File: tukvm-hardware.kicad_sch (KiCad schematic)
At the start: 19 parts, among them J1 PCIexpress_x1, J2 PCIexpress_bracket, J4 USB_C_Receptacle_USB2.0, U11 CH340N, U3 MCORE-H616

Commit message: Update pcb & sch for T113 SOM
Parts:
- removed R22: 33Ω, Resistor_SMD:R_0402_1005Metric, symbol Device:R_Small
- removed U3: MCORE-H616, tukvm:MCORE-H616, symbol tukvm:MCORE-H616
- added C23: 100uF 6.3V, Capacitor_SMD:C_1206_3216Metric, symbol Device:C_Small
- added C43: 10uF, Capacitor_SMD:C_0603_1608Metric, symbol Device:C_Small
- added SW1: SKRK, Button_Switch_SMD:SW_Push_SPST_NO_Alps_SKRK, symbol Switch:SW_Push
- added U3: TLT113-SOM, tukvm:SMD_140P_35X45_SOM_TLT113_PackageLength, symbol tukvm:TLT113-SOM
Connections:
- net +3.3V: now also C43.2, U3.135 (VDD_3V3_SOM)
- net +5V: now also C23.1, U3.139 (VDD_5V_SOM), U3.140 (VDD_5V_SOM)
- net ATX_PWR: now also U3.58 (PB2/LCD0_D0/I2S2_DOUT2/TWI0_SDA/I2S2_DIN2/LCD0_D18/UART4_TX/CAN0_TX0/PB_EINT2)
- net ATX_RST: now also U3.57 (PB12/DMIC_CLK/PWM0/SPDIF_IN/SPI1_CS/DBI_CSX/CLK_FANOUT2/IR_RX/PB_EINT12)
- net Earth: now also C23.2, C43.1, SW1.2, U3.106 (AGND_AUDIO), U3.116 (GND), U3.120 (GND), U3.128 (GND), U3.131 (GND), U3.134 (GND), U3.137 (GND), U3.138 (GND), U3.25 (GND), U3.33 (GND), U3.5 (GND), U3.52 (GND), U3.66 (GND), U3.71 (GND), U3.78 (GND), U3.85 (GND), U3.92 (GND), U3.97 (AGND_AUDIO)
- net HDD_LED: now also U3.46 (PE16/TWI3_SCK/D_JTAG_DO/PWM7/I2S0_BCLK/DMIC_DATA0/PE_EINT16)
- net HEART_BEAT_LED: now also U3.10 (PG8/UART1_RTS/TWI1_SCK/RGMII_RXD2/UART3_TX/PG_EINT8)
- net MS_STATUS: now also U3.91 (PD20/LCD0_HSYNC/TWI2_SCK/DMIC_CLK/PWM4/PD_EINT20)
- net MS_USBD+: now also U3.129 (USB1_DP)
- net MS_USBD-: now also U3.130 (USB1_DM)
- net OLED_SCL: now also U3.44 (PE14/TWI1_SCK/D_JTAG_MS/I2S0_DOUT1/I2S0_DIN0/DMIC_DATA2/RGMII_RXD3/PE_EINT14)
- net OLED_SDA: now also U3.45 (PE15/TWI1_SDA/D_JTAG_DI/PWM6/I2S0_LRCK/DMIC_DATA1/RGMII_RXCK/PE_EINT15)
- net OTG_D+: now also U3.132 (USB0_DP)
- net OTG_D-: now also U3.133 (USB0_DM)
- net PWR_LED: now also U3.47 (PE17/TWI3_SDA/D_JTAG_CK/IR_TX/I2S0_MCLK/DMIC_CLK/PE_EINT17)
- net SMCLK: now also U3.17 (PG6/UART1_TX/TWI2_SCK/RGMII_TXD2/PWM1/PG_EINT6)
- net SMDAT: now also U3.16 (PG7/UART1_RX/TWI2_SDA/RGMII_TXD3/SPDIF_IN/PG_EINT7)
- net TF_CLK: now also U3.29 (PF2/SDC0_CLK/UART0_TX/TWI0_SCK/LEDC_DO/SPDIF_IN/PF_EINT2)
- net TF_CMD: now also U3.31 (PF3/SDC0_CMD/JTAG_DO/R_JTAG_DO/I2S2_BCLK/PF_EINT3)
- net TF_D0: now also U3.28 (PF1/SDC0_D0/JTAG_DI/R_JTAG_DI/I2S2_DOUT0/I2S2_DIN1/PF_EINT1)
- net TF_D1: now also U3.27 (PF0/SDC0_D1/JTAG_MS/R_JTAG_MS/I2S2_DOUT1/I2S2_DIN0/PF_EINT0)
- net TF_D2: now also U3.30 (PF5/SDC0_D2/JTAG_CK/R_JTAG_CK/I2S2_LRCK/PF_EINT5)
- net TF_D3: now also U3.32 (PF4/SDC0_D3/UART0_RX/TWI0_SDA/PWM6/IR_TX/PF_EINT4)
- net TF_DET: now also U3.26 (PF6/SPDIF_OUT/IR_RX/I2S2_MCLK/PWM5/PF_EINT6)
- net U0RXD: now also U3.7 (PG18/UART2_RX/TWI3_SDA/PWM6/CLK_FANOUT1/SPDIF_OUT/UART0_RX/PG_EINT18)
- net U0TXD: now also U3.6 (PG17/UART2_TX/TWI3_SCK/PWM7/CLK_FANOUT0/IR_TX/UART0_TX/PG_EINT17)
- new net: SW1.1, U3.4 (RESET)
- new net M232_CTS: U3.55 (PB10/DMIC_DATA1/PWM7/TWI0_SCK/SPI1_MOSI/DBI_SDO/CLK_FANOUT0/UART1_RTS/PB_EINT10)
- new net M232_RTS: U3.56 (PB11/DMIC_DATA0/PWM2/TWI0_SDA/SPI1_CLK/DBI_SCLK/CLK_FANOUT1/UART1_CTS/PB_EINT11)
- new net M232_RXD: U3.53 (PB8/DMIC_DATA3/PWM5/TWI2_SCK/SPI1_HOLD/DBI_DCX/DBI_WRX/UART0_TX/UART1_TX/PB_EINT8)
- new net M232_TXD: U3.54 (PB9/DMIC_DATA2/PWM6/TWI2_SDA/SPI1_MISO/DBI_SDI/DBI_TE/DBI_DCX/UART0_RX/UART1_RX/PB_EINT9)
- new net MS_PWREN: U3.8 (PG13/I2S1_BCLK/TWI0_SDA/RGMII_CLKIN/RMII_RXER/PWM2/LEDC_DO/UART1_RX/PG_EINT13)
- new net RMII_CLK25M: U3.42 (PE10/NCSI0_D6/UART1_TX/PWM4/IR_RX/JTAG_DO/EPHY_25M/PE_EINT10)
- new net RMII_CRS_DV: U3.48 (PE0/NCSI0_HSYNC/UART2_RTS/TWI1_SCK/LCD0_HSYNC/RGMII_RXCTRL/RMII_CRS_DV/PE_EINT0)
- new net RMII_MDC: U3.40 (PE8/NCSI0_D4/UART1_RTS/PWM2/UART3_TX/JTAG_MS/MDC/PE_EINT8)
- new net RMII_MDIO: U3.41 (PE9/NCSI0_D5/UART1_CTS/PWM3/UART3_RX/JTAG_DI/MDIO/PE_EINT9)
- new net RMII_REFCLK: U3.51 (PE3/NCSI0_MCLK/UART2_RX/TWI0_SDA/CLK_FANOUT1/UART0_RX/RGMII_TXCK/RMII_TXCK/PE_EINT3)
- new net RMII_RXD0: U3.49 (PE1/NCSI0_VSYNC/UART2_CTS/TWI1_SDA/LCD0_VSYNC/RGMII_RXD0/RMII_RXD0/PE_EINT1)
- new net RMII_RXD1: U3.50 (PE2/NCSI0_PCLK/UART2_TX/TWI0_SCK/CLK_FANOUT0/UART0_TX/RGMII_RXD1/RMII_RXD1/PE_EINT2)
- new net RMII_RXER: U3.39 (PE7/NCSI0_D3/UART5_RX/TWI3_SDA/SPDIF_OUT/D_JTAG_CK/R_JTAG_CK/RGMII_CLKIN/RMII_RXER/PE_EINT7)
- new net RMII_TXD0: U3.36 (PE4/NCSI0_D0/UART4_TX/TWI2_SCK/CLK_FANOUT2/D_JTAG_MS/R_JTAG_MS/RGMII_TXD0/RMII_TXD0/PE_EINT4)
- new net RMII_TXD1: U3.37 (PE5/NCSI0_D1/UART4_RX/TWI2_SDA/LEDC_DO/D_JTAG_DI/R_JTAG_DI/RGMII_TXD1/RMII_TXD1/PE_EINT5)
- new net RMII_TXEN: U3.38 (PE6/NCSI0_D2/UART5_TX/TWI3_SCK/SPDIF_IN/D_JTAG_DO/R_JTAG_DO/RGMII_TXCTRL/RMII_TXEN/PE_EINT6)
- no-connect marks 34 -> 51
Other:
- sheet ETH PoE ports: added CLK25M, CRS_DV, MDC, MDIO, REFCLK, RXD0, RXD1, RXER, TXD0, TXD1, TXEN; removed ACT_LED, PHY_RD+, PHY_RD-, PHY_TD+, PHY_TD-, SPD_LED
- sheet GPIO ports: added M232_CTS, M232_RTS, M232_RXD, M232_TXD; removed none
- sheet HDMI IN ports: added PWR_EN; removed none
- moved on the sheet: C16, C32, C33, J1, J4, LED1, R18, R19, R20, R21, R23, R26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

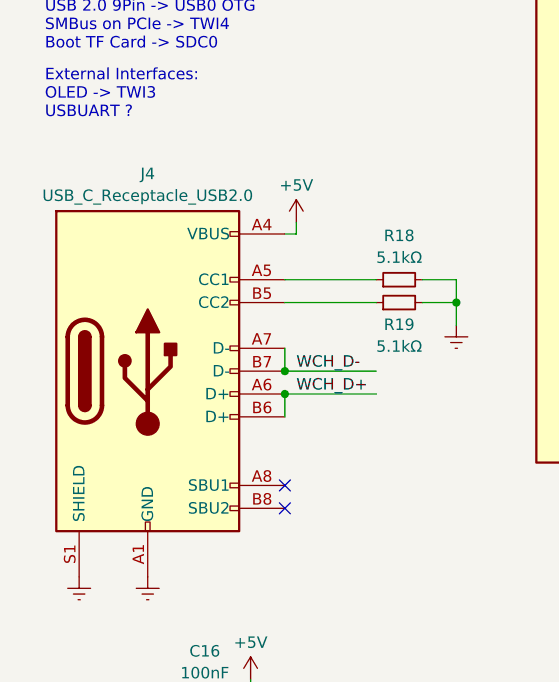
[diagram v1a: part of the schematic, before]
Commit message: Fix MS2109 symbol power pins, initial v1 release
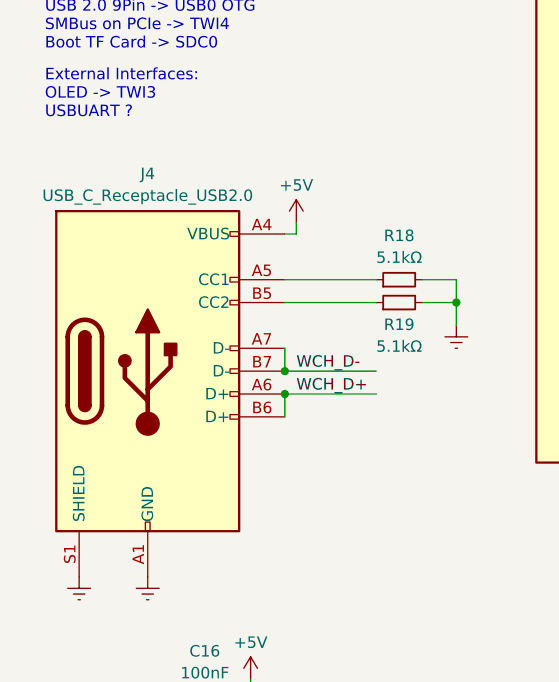
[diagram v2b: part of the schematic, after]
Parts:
- J4: symbol Connector:USB_C_Receptacle_USB2.0 -> Connector:USB_C_Receptacle_USB2.0_14P
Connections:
- no-connect marks 51 -> 49
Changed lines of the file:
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@@
-	)
-	(no_connect
-		(at 53.34 232.41)
 	)
 	(no_connect
@@
 	(no_connect
 		(at 205.74 27.94)
-	)
-	(no_connect
-		(at 53.34 234.95)
 	)
 	(wire
@@
 	)
 	(symbol
-		(lib_id "Connector:USB_C_Receptacle_USB2.0")
+		(lib_id "Connector:USB_C_Receptacle_USB2.0_14P")
 		(at 38.1 219.71 0)
 		(unit 1)
@@
 		(fields_autoplaced yes)
 		(property "Reference" "J4"
-			(at 38.1 197.7857 0)
+			(at 38.1 197.7855 0)
 			(effects
 				(font
@@
 		)
 		(property "Value" "USB_C_Receptacle_USB2.0"
-			(at 38.1 200.2099 0)
+			(at 38.1 200.2098 0)
 			(effects
 				(font
@@
 			)
 		)
-		(property "Description" ""
+		(property "Description" "USB 2.0-only 14P Type-C Receptacle connector"
 			(at 38.1 219.71 0)
 			(effects
@@
 		(pin "A7"
 		)
-		(pin "A8"
-		)
 		(pin "A9"
 		)
@@
 		(pin "B7"
 		)
-		(pin "B8"
-		)
 		(pin "B9"

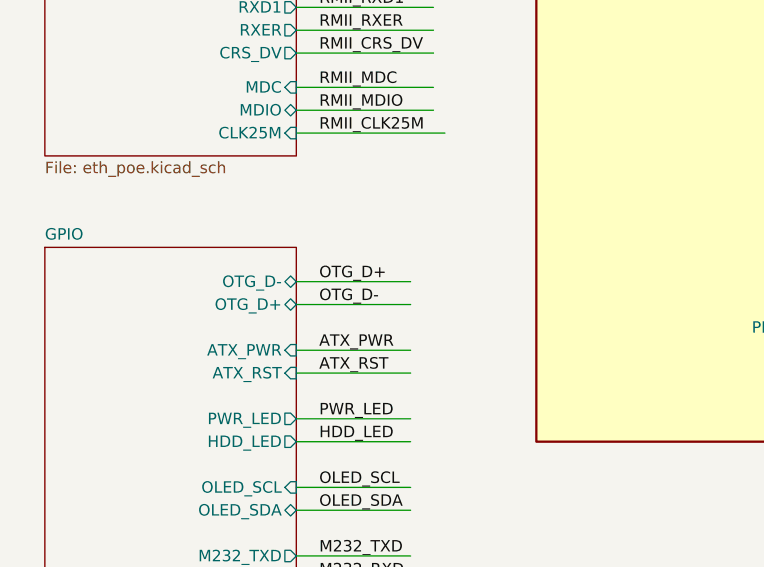
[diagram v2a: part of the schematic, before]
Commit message: Fix OTG USB polarity
Signed-off-by: Yichuan Gao <gaoyichuan000@gmail.com>
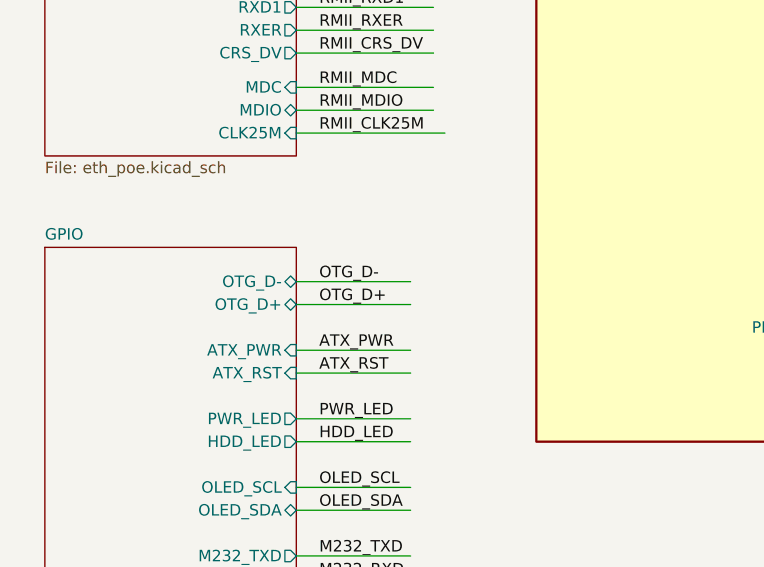
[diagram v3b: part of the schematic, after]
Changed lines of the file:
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@@
 	)
 	(label "OTG_D-"
-		(at 57.15 114.3 0)
+		(at 57.15 111.76 0)
 		(fields_autoplaced yes)
 		(effects
@@
 	)
 	(label "OTG_D+"
-		(at 57.15 111.76 0)
+		(at 57.15 114.3 0)
 		(fields_autoplaced yes)
 		(effects
